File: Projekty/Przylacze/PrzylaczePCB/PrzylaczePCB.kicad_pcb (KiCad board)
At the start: 2 copper layers, 150.1 x 110 mm, 116 parts, among them J1 Conn_02x04_Odd_Even, J2 Conn_02x20_Odd_Even, J3 Conn_01x06, J4 USB_B, J5 Screw_Terminal_01x06, Q1 BC557, Q10 BC557, Q11 BC547, Q12 BC547, Q2 BC547, Q3 BC557, Q4 BC547, Q5 2N3904, Q6 2N3904, Q7 BC557, Q8 BC557, Q9 2N7002, SW1 SW_Push, SW2 SW_SPDT, SW3 SW_SPDT, SW4 SW_SPDT, SW5 SW_SPDT, SW6 SW_SPDT, SW7 SW_SPDT, SW8 SW_SPDT, SW9 SW_SPDT, U1 74AHC1G04, U10 LDL1117S33R, U2 74AHC1G04, U3 ATSAM4S2AA-AU, U4 MAX3485, U6 MCP2561-E-P, U7 TJA1055T_3_C,518, U8 MCP2515-xSO, U9 DI78M05UAB, Y1 20MHz

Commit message: Przyłącze - projekt PCB v0.2
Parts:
- removed REF** (x4): MountingHole_3.2mm_M3, MountingHole:MountingHole_3.2mm_M3
- D10, D8, D9: footprint 1_Librar:2PAD_WIRE -> 1_WLASNA_Library:2PAD_WIRE; moved to B.Cu
- D11, D4, Q9, SEL5, SEL6, U10, U3, U4, U7, Y1: moved to B.Cu
- D3, D5: footprint 1_Librar:2PAD_WIRE -> 1_WLASNA_Library:2PAD_WIRE
- H1: footprint 1_Librar:4Pin_COMMON_MODE_CHOKE_B82787C0104H002 -> 1_WLASNA_Library:4Pin_COMMON_MODE_CHOKE_B82787C0104H002; moved to B.Cu
- J2: footprint Connector_PinHeader_2.54mm:PinHeader_2x20_P2.54mm_Vertical -> Connector_PinHeader_2.54mm:PinHeader_2x20_P2.54mm_Horizontal
- SW2, SW3, SW4, SW5, SW6, SW7, SW8, SW9: footprint 1_Librar:3PAD_WIRE_SWITCH -> 1_WLASNA_Library:3PAD_WIRE_SWITCH; moved to B.Cu
- moved J5 182.2 mm to (243.3, 155.7)
- moved SW1 152.8 mm to (24.3, 186.5), turned to 0 degrees
- moved R9 149.2 mm to (71.9, 187.9)
- moved R14 144.8 mm to (149.9, 150.6)
- moved U1 142.0 mm to (91.9, 167.2)
- moved C2 139.8 mm to (17.7, 174.4), turned to 0 degrees
- moved R7 139.7 mm to (71.9, 179.8)
- moved C3 139.4 mm to (17.7, 182.6)
- moved R3 138.1 mm to (71.9, 163.6)
- moved R10 138.1 mm to (71.9, 191.9), turned to 0 degrees
- moved D1 134.5 mm to (83.3, 167.8), turned to 90 degrees
- moved Q5 132.3 mm to (96.1, 156.7), turned to 0 degrees
- moved Q1 132.0 mm to (83.1, 156.7)
- moved U3 131.4 mm to (27.9, 176.8)
- moved D2 131.2 mm to (87.6, 167.8), turned to 90 degrees
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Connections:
- J5 pad 3: CANH -> CANL
- J5 pad 4: CANL -> CANH
- R15 pad 2: RX/TX ENABLE  -> RX/TX ENABLE
- R16 pad 1: RX/TX ENABLE  -> RX/TX ENABLE
- R19 pad 1: RX/TX ENABLE  -> RX/TX ENABLE
- R23 pad 2: RX/TX ENABLE  -> RX/TX ENABLE
- Y1 pad 1: Net-(U8-OSC1) -> Net-(U8-OSC2)
- Y1 pad 2: Net-(U8-OSC2) -> Net-(U8-OSC1)
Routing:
- net GND: track 531.7 -> 253.4 mm, vias 2 -> 0
- net +5V: track 259.2 -> 23.5 mm, vias 3 -> 0
- net STB_FT: track 105.8 -> 13.1 mm, vias 2 -> 0
- net CANL: track 99.2 -> 15.3 mm, vias 1 -> 0
- net CANH: track 96.7 -> 15.3 mm, vias 1 -> 0
- net RX0BF: track 65.8 -> 0.00 mm
- net OPTO_R2: track 60.7 -> 0.00 mm, vias 1 -> 0
- net OPTO_SW2: track 56.5 -> 0.00 mm, vias 3 -> 0
- net RX/TX ENABLE : track 55.1 -> 0.00 mm
- net RX1BF: track 49.9 -> 0.00 mm
- net OPTO_SW1: track 49.4 -> 0.00 mm, vias 1 -> 0
- net Net-(D7-K): track 58.8 -> 9.75 mm
- net WAKE: track 59.3 -> 12.0 mm
- net OPTO_R1: track 44.0 -> 0.00 mm, vias 1 -> 0
- net Net-(D1-A): track 42.9 -> 0.00 mm, vias 2 -> 0
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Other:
- board size 150.1 x 110 mm -> 154.9 x 88.9 mm

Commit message: Przyłącze - projekt PCB v0.3
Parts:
- D3, D5, U9: moved to B.Cu
- J3: footprint Connector_PinHeader_2.54mm:PinHeader_1x06_P2.54mm_Horizontal -> Connector_PinHeader_2.54mm:PinHeader_1x06_P2.54mm_Vertical
- moved D2 217.1 mm to (-128.0, 143.0)
- moved Q3 217.1 mm to (-126.1, 131.9)
- moved Q4 217.1 mm to (-126.1, 137.7)
- moved Q7 217.1 mm to (-113.1, 131.9)
- moved Q8 217.1 mm to (-113.1, 137.7)
- moved R1 217.1 mm to (-143.8, 130.6)
- moved R10 217.1 mm to (-143.8, 167.1)
- moved R2 217.1 mm to (-143.8, 134.7)
- moved R3 217.1 mm to (-143.8, 138.7)
- moved R4 217.1 mm to (-143.8, 142.8)
- moved R5 217.1 mm to (-143.8, 146.8)
- moved R6 217.1 mm to (-143.8, 150.9)
- moved R7 217.1 mm to (-143.8, 154.9)
- moved R8 217.1 mm to (-143.8, 159.0)
- moved R9 217.1 mm to (-143.8, 163.0)
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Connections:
- J5 pad 1: A -> CANH
- J5 pad 2: B -> CANL
- J5 pad 3: CANL -> B
- J5 pad 4: CANH -> A
- U10 pad 1: (no net) -> GND
- U3 pad 33: +3.3V -> unconnected-(U3-VDDIO-Pad33)
- U3 pad 41: Net-(U3-VDDOUT) -> unconnected-(U3-VDDCORE-Pad41)
- U3 pad 47: +3.3V -> unconnected-(U3-VDDIO-Pad47)
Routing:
- net GND: track 253.4 -> 567.9 mm, vias 0 -> 2
- net Net-(D7-K): track 9.75 -> 128.0 mm
- net +12V: track 4.73 -> 90.3 mm
- net +5V: track 23.5 -> 103.8 mm
- net ERR: track 0.00 -> 69.8 mm, vias 0 -> 2
- net +3.3V: track 133.6 -> 202.9 mm
- net A: track 44.5 -> 93.1 mm
- net RXD: track 70.8 -> 109.4 mm
- net B: track 44.0 -> 82.4 mm
- net TXD: track 50.0 -> 86.4 mm
- net CANH: track 15.3 -> 42.3 mm
- net CANL: track 15.3 -> 38.1 mm
- net TX_MCU: track 7.40 -> 27.5 mm
- net Net-(D12-K): track 36.0 -> 53.2 mm
- net Net-(U3-VDDOUT): track 0.00 -> 13.9 mm
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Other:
- board outline removed

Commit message: Przyłącze - projekt PCB v0.4
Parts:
- added REF**: MountingHole_3.2mm_M3, MountingHole:MountingHole_3.2mm_M3, F.Cu at (44.2, 76.2)
- added REF**: MountingHole_3.2mm_M3, MountingHole:MountingHole_3.2mm_M3, F.Cu at (44.2, 193.0)
- added REF**: MountingHole_3.2mm_M3, MountingHole:MountingHole_3.2mm_M3, F.Cu at (170.7, 193.0)
- added REF**: MountingHole_3.2mm_M3, MountingHole:MountingHole_3.2mm_M3, F.Cu at (170.7, 76.2)
- D1, D2, U1, U2: moved to B.Cu
- U3: moved to F.Cu
- moved J3 303.3 mm to (55.6, 136.1), turned to 90 degrees
- moved J4 278.9 mm to (51.3, 106.6), turned to 180 degrees
- moved R14 267.7 mm to (65.8, 113.3), turned to 180 degrees
- moved R13 264.4 mm to (65.8, 108.7), turned to 180 degrees
- moved R12 261.0 mm to (63.8, 105.2), turned to 180 degrees
- moved R11 259.2 mm to (62.2, 100.6), turned to 180 degrees
- moved R5 217.2 mm to (70.0, 185.1), turned to 180 degrees
- moved R7 215.4 mm to (70.0, 181.7), turned to 90 degrees
- moved R6 214.1 mm to (70.3, 157.8), turned to 180 degrees
- moved R8 213.8 mm to (70.0, 154.3), turned to 90 degrees
- moved R10 210.0 mm to (65.4, 148.7), turned to 90 degrees
- moved R9 209.6 mm to (65.4, 176.1), turned to 90 degrees
- moved R3 200.8 mm to (52.2, 182.2), turned to 90 degrees
- moved R1 198.0 mm to (47.4, 182.2), turned to 90 degrees
- moved Q1 197.4 mm to (58.4, 181.6), turned to 90 degrees
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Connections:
- J3 pad 1: GND -> Net-(J3-Pin_1)
- J3 pad 6: Net-(J3-Pin_6) -> GND
- U3 pad 25: Net-(J3-Pin_4) -> Net-(J3-Pin_1)
- U3 pad 32: OPTO_R1 -> OPTO_SW2
- U3 pad 35: OPTO_SW2 -> OPTO_R1
- U3 pad 37: Net-(J3-Pin_5) -> Net-(J3-Pin_2)
- U3 pad 38: Net-(J3-Pin_2) -> Net-(J3-Pin_3)
- U3 pad 39: Net-(J3-Pin_6) -> Net-(J3-Pin_4)
- U3 pad 40: Net-(J3-Pin_3) -> Net-(J3-Pin_5)
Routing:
- net GND: track 567.9 -> 719.3 mm, vias 2 -> 0
- net OPTO_R2: track 0.00 -> 101.5 mm
- net OPTO_SW2: track 0.00 -> 83.1 mm
- net +5V: track 103.8 -> 185.8 mm
- net OPTO_R1: track 0.00 -> 70.1 mm
- net OPTO_SW1: track 0.00 -> 51.6 mm
- net Net-(U3-DDM/PB10): track 0.00 -> 34.6 mm, vias 0 -> 1
- net Net-(U3-DDP/PB11): track 0.00 -> 29.9 mm, vias 0 -> 1
- net Net-(D2-A): track 0.00 -> 24.7 mm
- net Net-(D1-A): track 0.00 -> 24.2 mm
- net +3.3V: track 202.9 -> 179.5 mm
- net Net-(J3-Pin_1): track 0.00 -> 17.9 mm
- net USBMON: track 4.57 -> 21.6 mm, vias 0 -> 1
- net Net-(Q2-B): track 0.00 -> 13.2 mm
- net Net-(Q4-B): track 0.00 -> 12.8 mm
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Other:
- board outline added: 134.6 x 125 mm

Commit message: Przyłącze - projekt PCB v0.5
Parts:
- moved R32 12.0 mm to (159.5, 112.8), turned to 90 degrees
- moved R43 11.5 mm to (130.0, 119.4), turned to -90 degrees
- moved D8 4.46 mm to (166.3, 111.3)
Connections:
- J2 pad 1: A -> OPTO_R1
- J2 pad 10: TX_MCU -> SPCK
- J2 pad 11: RXD -> UART0_TX
- J2 pad 12: RX_MCU -> UART0_RX
- J2 pad 13: STB_FT -> TX0RTS
- J2 pad 14: RX/TX ENABLE -> TX_MCU
- J2 pad 15: WAKE -> TX1RTS
- J2 pad 16: OPTO_SW1 -> RX_MCU
- J2 pad 17: EN -> TX2RTS
- J2 pad 18: OPTO_SW2 -> RX/TX ENABLE
- J2 pad 19: ERR -> RX0BF
- J2 pad 2: A -> OPTO_SW1
- J2 pad 20: OPTO_R1 -> TXD
- J2 pad 21: TX0RTS -> RX1BF
- J2 pad 22: OPTO_R2 -> RXD
- J2 pad 23: TX1RTS -> SOF
- J2 pad 24: UART0_RX -> STB_FT
- J2 pad 25: TX2RTS -> INT
- J2 pad 26: UART0_TX -> WAKE
- J2 pad 27: RX0BF -> RESET
- J2 pad 28: MOSI -> EN
- J2 pad 29: RX1BF -> unconnected-(J2-Pin_29-Pad29)
- J2 pad 3: B -> OPTO_R2
- J2 pad 30: MISO -> ERR
- J2 pad 31: SOF -> unconnected-(J2-Pin_31-Pad31)
- J2 pad 32: SPCK -> unconnected-(J2-Pin_32-Pad32)
- J2 pad 33: INT -> A
- J2 pad 34: CS3 -> A
- J2 pad 35: RESET -> B
- J2 pad 36: CS0 -> B
- J2 pad 37: unconnected-(J2-Pin_37-Pad37) -> CANL
- J2 pad 38: unconnected-(J2-Pin_38-Pad38) -> CANL
- J2 pad 39: unconnected-(J2-Pin_39-Pad39) -> CANH
- J2 pad 4: B -> OPTO_SW2
- J2 pad 40: unconnected-(J2-Pin_40-Pad40) -> CANH
- J2 pad 5: CANH -> CS3
- J2 pad 6: CANH -> MOSI
- J2 pad 7: CANL -> CS0
- J2 pad 8: CANL -> MISO
- J2 pad 9: TXD -> unconnected-(J2-Pin_9-Pad9)
- U3 pad 28: RX/TX ENABLE  -> RX/TX ENABLE
- U3 pad 34: GND -> unconnected-(U3-GND-Pad34)
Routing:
- net CANH: track 42.3 -> 243.2 mm, vias 0 -> 1
- net CANL: track 38.1 -> 226.2 mm, vias 0 -> 1
- net B: track 82.4 -> 262.1 mm, vias 0 -> 1
- net A: track 93.1 -> 269.0 mm, vias 0 -> 1
- net CS0: track 0.00 -> 171.3 mm, vias 0 -> 3
- net MOSI: track 0.00 -> 150.4 mm, vias 0 -> 3
- net SPCK: track 0.00 -> 148.1 mm, vias 0 -> 3
- net MISO: track 0.00 -> 145.0 mm, vias 0 -> 3
- net RADIO_IRQ: track 0.00 -> 133.4 mm, vias 0 -> 1
- net +5V: track 185.8 -> 305.9 mm, vias 0 -> 1
- net RX_MCU: track 2.96 -> 89.6 mm, vias 0 -> 1
- net TX_MCU: track 27.5 -> 112.8 mm
- net +3.3V: track 179.5 -> 258.2 mm, vias 0 -> 1
- net GND: track 719.3 -> 794.5 mm
- net +12V: track 90.3 -> 76.9 mm
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
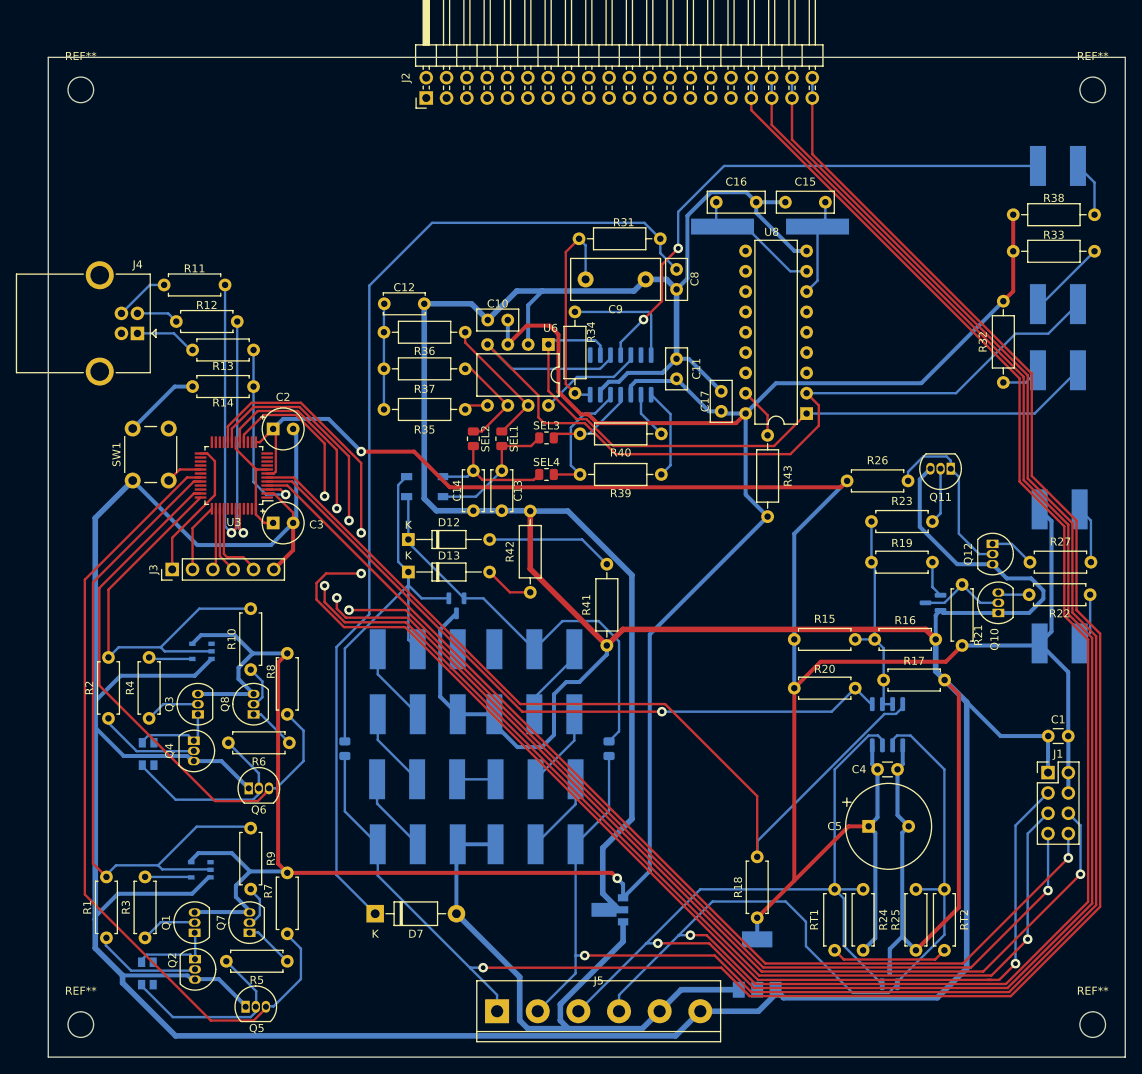
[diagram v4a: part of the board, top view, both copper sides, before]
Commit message: Przyłącze - projekt PCB v1.0
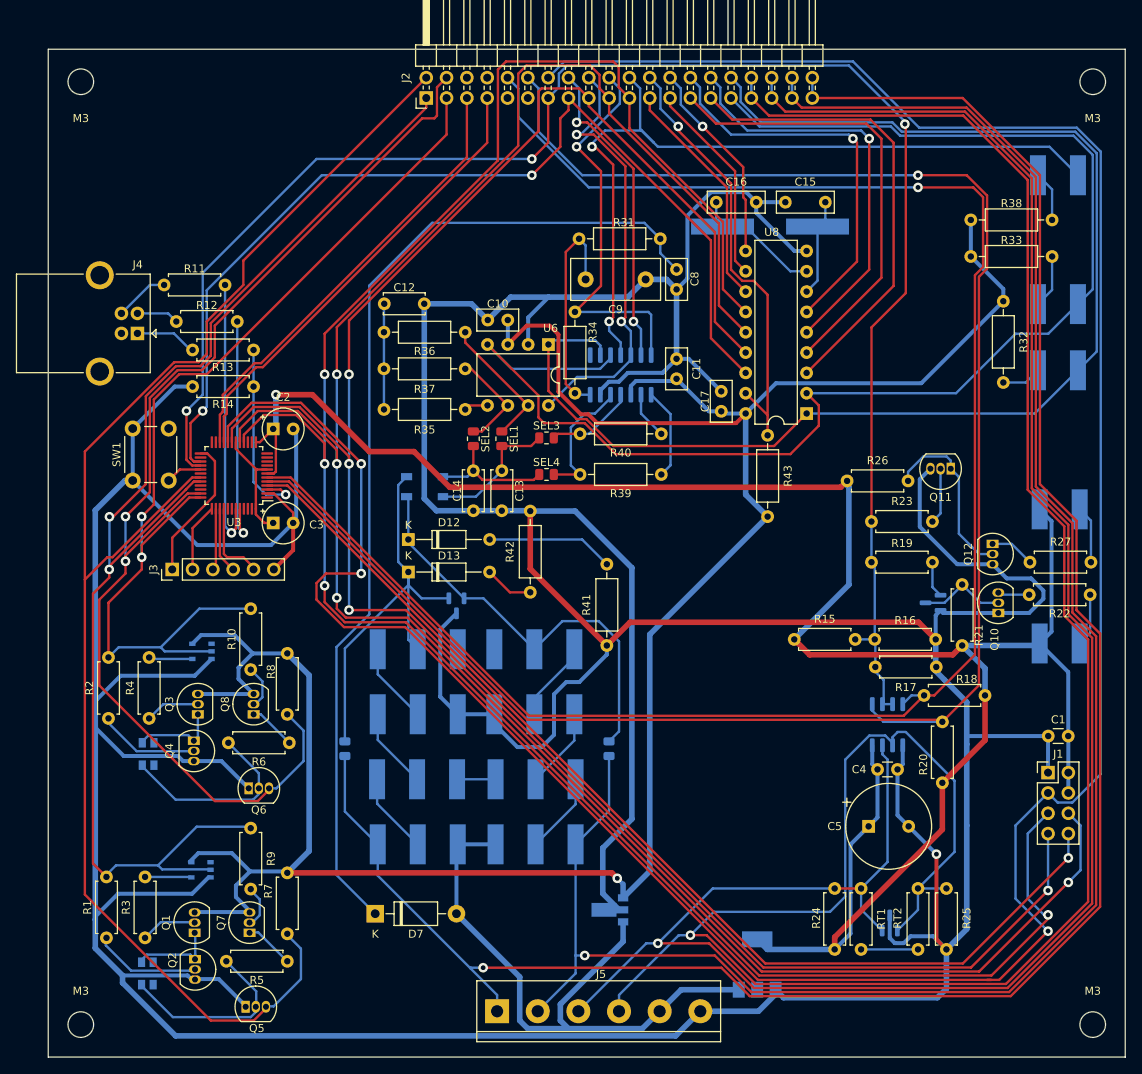
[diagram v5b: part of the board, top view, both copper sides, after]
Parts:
- moved R18 39.8 mm to (157.2, 151.9), turned to 180 degrees
- moved R20 22.0 mm to (151.9, 162.8), turned to 90 degrees
- moved D4 6.71 mm to (145.3, 180.3)
- moved R33 5.34 mm to (165.6, 97.0)
- moved R38 5.34 mm to (165.6, 92.5)
- moved R25 3.81 mm to (152.4, 176.0)
- moved R24 3.56 mm to (138.4, 183.6)
- moved RT2 3.30 mm to (148.8, 183.6)
- moved RT1 3.30 mm to (141.7, 176.0)
- moved R17 1.94 mm to (143.5, 148.3)
- moved D10 1.16 mm to (166.3, 86.9), turned to 180 degrees
- moved M3 1.02 mm to (44.2, 75.2)
- moved M3 1.02 mm to (170.7, 75.2)
- renumbered REF** to M3
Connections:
- J2 pad 1: OPTO_R1 -> OPTO_SW2
- J2 pad 10: SPCK -> TX_MCU
- J2 pad 11: UART0_TX -> unconnected-(J2-Pin_11-Pad11)
- J2 pad 12: UART0_RX -> RX_MCU
- J2 pad 13: TX0RTS -> RX/TX ENABLE
- J2 pad 14: TX_MCU -> CS0
- J2 pad 15: TX1RTS -> CS3
- J2 pad 16: RX_MCU -> EN
- J2 pad 17: TX2RTS -> MISO
- J2 pad 18: RX/TX ENABLE -> STB_FT
- J2 pad 19: RX0BF -> MOSI
- J2 pad 2: OPTO_SW1 -> OPTO_R2
- J2 pad 20: TXD -> WAKE
- J2 pad 21: RX1BF -> SPCK
- J2 pad 22: RXD -> ERR
- J2 pad 23: SOF -> INT
- J2 pad 24: STB_FT -> RESET
- J2 pad 25: INT -> RX0BF
- J2 pad 26: WAKE -> RX1BF
- J2 pad 27: RESET -> TX0RTS
- J2 pad 28: EN -> TX2RTS
- J2 pad 29: unconnected-(J2-Pin_29-Pad29) -> SOF
- J2 pad 3: OPTO_R2 -> OPTO_SW1
- J2 pad 30: ERR -> TX1RTS
- J2 pad 31: unconnected-(J2-Pin_31-Pad31) -> RXD
- J2 pad 32: unconnected-(J2-Pin_32-Pad32) -> TXD
- J2 pad 4: OPTO_SW2 -> OPTO_R1
- J2 pad 5: CS3 -> UART0_RX
- J2 pad 6: MOSI -> unconnected-(J2-Pin_6-Pad6)
- J2 pad 7: CS0 -> UART0_TX
- J2 pad 8: MISO -> unconnected-(J2-Pin_8-Pad8)
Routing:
- net RX/TX ENABLE: track 27.2 -> 211.0 mm, vias 0 -> 3
- net CS0: track 171.3 -> 340.7 mm
- net RX_MCU: track 89.6 -> 241.8 mm
- net CS3: track 0.00 -> 124.9 mm, vias 0 -> 2
- net SPCK: track 148.1 -> 272.9 mm, vias 3 -> 4
- net MOSI: track 150.4 -> 270.3 mm, vias 3 -> 4
- net TX_MCU: track 112.8 -> 232.4 mm, vias 0 -> 1
- net MISO: track 145.0 -> 259.4 mm, vias 3 -> 4
- net OPTO_R2: track 101.5 -> 183.7 mm
- net OPTO_R1: track 70.1 -> 150.3 mm, vias 0 -> 2
- net TXD: track 86.9 -> 165.7 mm
- net OPTO_SW2: track 83.1 -> 160.4 mm, vias 0 -> 2
- net OPTO_SW1: track 51.6 -> 127.7 mm, vias 0 -> 2
- net RXD: track 111.0 -> 178.6 mm
- net SOF: track 0.00 -> 58.4 mm
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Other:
- board size 134.6 x 125 mm -> 134.6 x 126 mm

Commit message: Przyłącze - projekt PCB v1.1
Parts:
- added C10: 100n, Capacitor_THT:C_Disc_D5.0mm_W2.5mm_P2.50mm, F.Cu at (55.5, 126.7)
- added C11: 100n, Capacitor_THT:C_Disc_D5.0mm_W2.5mm_P2.50mm, F.Cu at (73.6, 125.9)
- added C12: 100n, Capacitor_THT:C_Disc_D5.0mm_W2.5mm_P2.50mm, F.Cu at (68.5, 118.4)
- added C13: 100n, Capacitor_THT:C_Disc_D5.0mm_W2.5mm_P2.50mm, F.Cu at (70.7, 122.8)
- added C14: 100n, Capacitor_THT:C_Disc_D5.0mm_W2.5mm_P2.50mm, F.Cu at (64.2, 116.7)
- added C15: 100n, Capacitor_THT:C_Disc_D5.0mm_W2.5mm_P2.50mm, F.Cu at (71.9, 134.7)
- added C16: 100n, Capacitor_THT:C_Disc_D5.0mm_W2.5mm_P2.50mm, F.Cu at (71.5, 131.6)
- added C22: 330n, Capacitor_THT:C_Disc_D5.0mm_W2.5mm_P2.50mm, F.Cu at (130.0, 171.0)
- added C23: 100n, Capacitor_THT:C_Disc_D5.0mm_W2.5mm_P2.50mm, F.Cu at (130.1, 160.1)
- added C24: 1u, Capacitor_THT:CP_Radial_D5.0mm_P2.00mm, F.Cu at (120.1, 184.5)
- added C25: 4.7u, Capacitor_THT:CP_Radial_D5.0mm_P2.00mm, F.Cu at (128.7, 178.9)
- added L1: 10u, Inductor_SMD:L_1206_3216Metric_Pad1.22x1.90mm_HandSolder, F.Cu at (68.4, 130.6)
- D4: renamed from D10; footprint 1_WLASNA_Library:2PAD_WIRE -> Connector_PinHeader_2.54mm:PinHeader_1x02_P2.54mm_Vertical
- D5: renamed from D8; footprint 1_WLASNA_Library:2PAD_WIRE -> Connector_PinHeader_2.54mm:PinHeader_1x02_P2.54mm_Vertical
- D6: renamed from D9; footprint 1_WLASNA_Library:2PAD_WIRE -> Connector_PinHeader_2.54mm:PinHeader_1x02_P2.54mm_Vertical
- D7: renamed from D5; footprint 1_WLASNA_Library:2PAD_WIRE -> Connector_PinHeader_2.54mm:PinHeader_1x02_P2.54mm_Vertical
- D8: renamed from D3; footprint 1_WLASNA_Library:2PAD_WIRE -> Connector_PinHeader_2.54mm:PinHeader_1x02_P2.54mm_Vertical
- H1: footprint 1_WLASNA_Library:4Pin_COMMON_MODE_CHOKE_B82787C0104H002 -> PrzylaczeFootprintLibrary:4Pin_COMMON_MODE_CHOKE_B82787C0104H002
- Q1: renamed from Q12; footprint Package_TO_SOT_THT:TO-92_Inline -> Package_TO_SOT_THT:TO-92L_HandSolder
- Q10: renamed from Q7; footprint Package_TO_SOT_THT:TO-92_Inline -> Package_TO_SOT_THT:TO-92L_HandSolder
- Q11: renamed from Q5; footprint Package_TO_SOT_THT:TO-92_Inline -> Package_TO_SOT_THT:TO-92L_HandSolder
- Q2: renamed from Q11; footprint Package_TO_SOT_THT:TO-92_Inline -> Package_TO_SOT_THT:TO-92L_HandSolder
- Q3: renamed from Q4; footprint Package_TO_SOT_THT:TO-92_Inline -> Package_TO_SOT_THT:TO-92L_HandSolder
- Q4: renamed from Q3; footprint Package_TO_SOT_THT:TO-92_Inline -> Package_TO_SOT_THT:TO-92L_HandSolder
- Q5: renamed from Q6; footprint Package_TO_SOT_THT:TO-92_Inline -> Package_TO_SOT_THT:TO-92L_HandSolder
- Q6: renamed from Q8; footprint Package_TO_SOT_THT:TO-92_Inline -> Package_TO_SOT_THT:TO-92L_HandSolder
- Q7: renamed from Q10; footprint Package_TO_SOT_THT:TO-92_Inline -> Package_TO_SOT_THT:TO-92L_HandSolder
- Q8: renamed from Q2; footprint Package_TO_SOT_THT:TO-92_Inline -> Package_TO_SOT_THT:TO-92L_HandSolder
- Q9: renamed from Q1; footprint Package_TO_SOT_THT:TO-92_Inline -> Package_TO_SOT_THT:TO-92L_HandSolder
- SW2, SW5, SW6, SW9: footprint 1_WLASNA_Library:3PAD_WIRE_SWITCH -> Connector_PinHeader_2.54mm:PinHeader_1x03_P2.54mm_Vertical
- SW3: renamed from SW4; footprint 1_WLASNA_Library:3PAD_WIRE_SWITCH -> Connector_PinHeader_2.54mm:PinHeader_1x03_P2.54mm_Vertical
- SW4: renamed from SW3; footprint 1_WLASNA_Library:3PAD_WIRE_SWITCH -> Connector_PinHeader_2.54mm:PinHeader_1x03_P2.54mm_Vertical
- SW7: renamed from SW8; footprint 1_WLASNA_Library:3PAD_WIRE_SWITCH -> Connector_PinHeader_2.54mm:PinHeader_1x03_P2.54mm_Vertical
- SW8: renamed from SW7; footprint 1_WLASNA_Library:3PAD_WIRE_SWITCH -> Connector_PinHeader_2.54mm:PinHeader_1x03_P2.54mm_Vertical
- moved U8 23.1 mm to (128.0, 164.3)
- moved SW4 14.0 mm to (80.8, 159.0), turned to -90 degrees
- moved SW2 13.3 mm to (97.4, 159.0), turned to 90 degrees
- moved C19 11.8 mm to (69.2, 142.0)
- moved SW3 9.28 mm to (97.4, 162.8), turned to 90 degrees
- moved SW5 8.60 mm to (85.9, 162.8), turned to 90 degrees
- moved C1 7.65 mm to (69.7, 111.1)
- moved D7 6.96 mm to (166.6, 121.7)
- moved SW8 6.96 mm to (80.8, 166.8), turned to -90 degrees
- moved SW6 5.73 mm to (97.4, 166.8), turned to 90 degrees
- moved SW9 5.47 mm to (80.8, 170.7), turned to -90 degrees
- moved SW1 4.10 mm to (47.5, 122.5)
- moved SW7 3.66 mm to (97.4, 170.7), turned to 90 degrees
- moved Q8 2.14 mm to (56.3, 184.8)
- moved Q3 1.78 mm to (56.6, 157.2)
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- renumbered C2 to C1, C14 to C17, C13 to C18, C3 to C19, C12 to C2, C4 to C20, C1 to C21, C5 to C26, C10 to C3, C16 to C4, C15 to C5, C9 to C6, C11 to C7, C17 to C8, C8 to C9, D13 to D1, D2 to D10, D4 to D11, D1 to D12, D12 to D2, D7 to D3, D11 to D9, J2 to J1, J4 to J2, J1 to J4, Q9 to Q12, R11 to R1, R33 to R10, R38 to R11, R42 to R12, R35 to R13, R43 to R14, R40 to R15, R39 to R16, R26 to R17, R19 to R18, R23 to R19, R13 to R2, R27 to R20, R22 to R21, R2 to R22, R4 to R23, R6 to R24, R10 to R25, R8 to R26, R41 to R27, R15 to R28, R18 to R29, R37 to R3, R16 to R30, R20 to R31, R21 to R32, R17 to R33, R1 to R34, R3 to R35, R5 to R36, R7 to R37, R9 to R38, R24 to R39, R14 to R4, R25 to R40, R12 to R5, R31 to R6, R34 to R7, R36 to R8, R32 to R9, SEL3 to SEL1, SEL4 to SEL3, SEL1 to SEL4, SEL6 to SEL5, SEL5 to SEL6, U6 to U1, U3 to U2, U8 to U3, U7 to U4, U4 to U5, U2 to U6, U10 to U7, U9 to U8, U1 to U9
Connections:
- C19 pad 1: Net-(U3-VDDOUT) -> Net-(U2-VDDOUT)
- U2 pad 18: Net-(U3-VDDOUT) -> Net-(U2-VDDOUT)
- U2 pad 33: unconnected-(U3-VDDIO-Pad33) -> +3.3V
- U2 pad 34: unconnected-(U3-GND-Pad34) -> GND
- U2 pad 41: unconnected-(U3-VDDCORE-Pad41) -> Net-(U2-VDDOUT)
- U2 pad 47: unconnected-(U3-VDDIO-Pad47) -> +3.3V
- U2 pad 48: Net-(U3-VDDOUT) -> Net-(U2-VDDPLL)
- U2 pad 8: Net-(U3-VDDOUT) -> Net-(U2-VDDOUT)
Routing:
- net GND: track 771.2 -> 17.0 mm, vias 1 -> 16
- net +3.3V: track 268.8 -> 349.0 mm
- net Net-(U2-VDDOUT): track 0.00 -> 44.5 mm
- net +12V: track 76.9 -> 118.4 mm
- net SPCK: track 272.9 -> 291.1 mm
- net +5V: track 307.4 -> 325.6 mm
- net CANL: track 238.3 -> 253.7 mm
- net Net-(U3-VDDOUT): track 14.1 -> 0.00 mm
- net CS0: track 340.7 -> 354.2 mm
- net MOSI: track 270.3 -> 283.3 mm
- net Net-(D2-K): track 53.2 -> 66.2 mm
- net MISO: track 259.4 -> 271.8 mm
- net A: track 288.4 -> 300.3 mm
- net TXD: track 165.7 -> 175.9 mm
- net CANH: track 254.2 -> 264.2 mm
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- added copper zone on B.Cu, net +3.3V
- added copper zone on B.Cu, net GND
- added copper zone on F.Cu, net GND

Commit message: Przyłącze - projekt PCB v1.2
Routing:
- net OPTO_R1: track 155.9 -> 164.8 mm
- net +3.3V: track 349.0 -> 355.7 mm
- net OPTO_SW1: track 134.1 -> 139.0 mm
- net +12V: track 118.4 -> 122.7 mm
- net CANH: track 264.2 -> 268.4 mm
- net OPTO_R2: track 189.7 -> 186.2 mm
- net ERR: track 97.3 -> 100.8 mm
- net STB_FT: track 54.3 -> 57.1 mm
- net RXD: track 187.8 -> 190.7 mm
- net Net-(U2-VDDOUT): track 44.5 -> 47.0 mm
- net WAKE: track 51.0 -> 53.1 mm
- net CANL: track 253.7 -> 255.8 mm
- net Net-(D6-A): track 10.6 -> 8.71 mm
- net MOSI: track 283.3 -> 281.5 mm
- net EN: track 39.4 -> 41.2 mm
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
